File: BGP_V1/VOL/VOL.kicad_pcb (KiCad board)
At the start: 2 copper layers, 60 x 30 mm, 33 parts, among them IC1 TC7660SO-08, P1 CONN_01X03, P2 CONN_01X02, P3 CONN_01X05, P4 CONN_01X05, P5 CONN_01X05, P6 Conn_01x14, P7 CONN_02X02, U1 OPA2170

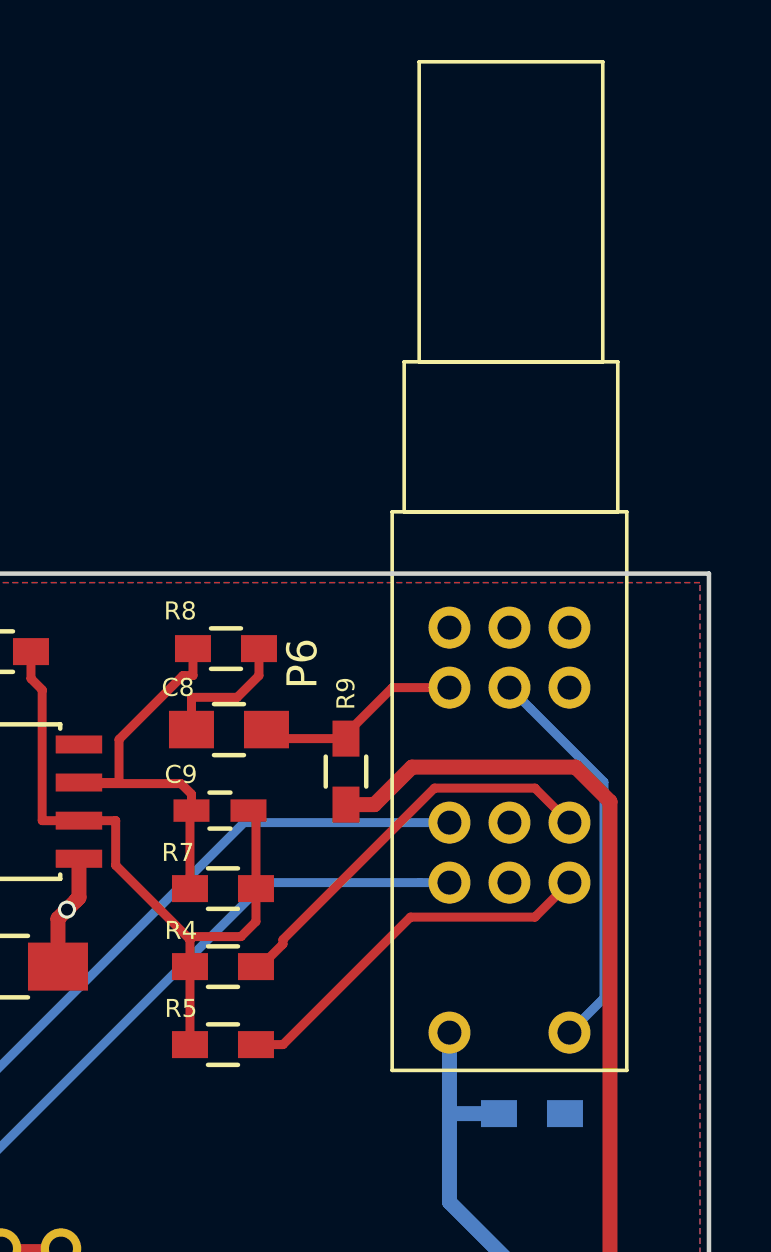
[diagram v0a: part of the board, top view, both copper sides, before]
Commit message: Pot fixups for silkscreen overlap
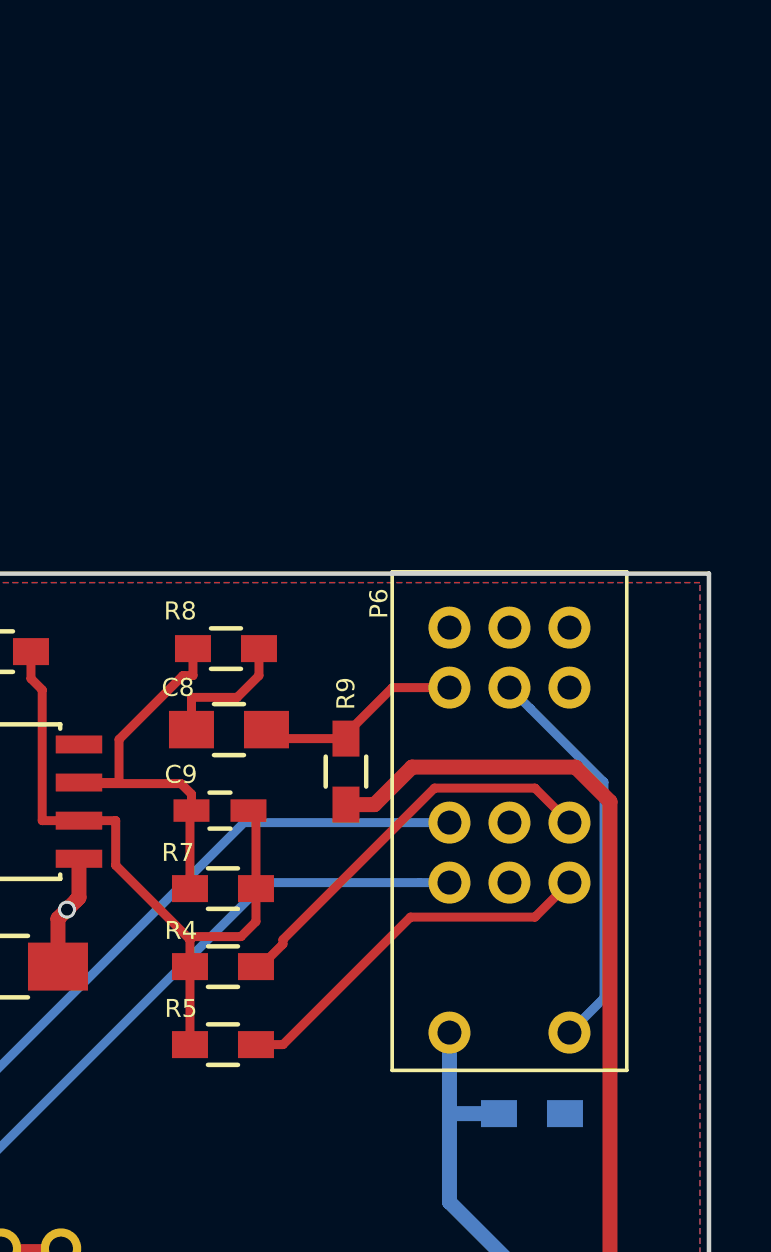
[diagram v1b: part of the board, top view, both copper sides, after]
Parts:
- moved P6 4.25 mm to (174.3, 82.8)
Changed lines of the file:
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@@
     (links 70)
     (no_connects 0)
-    (area 118.924999 63.424999 179.303001 112.85588)
+    (area 118.924999 80.424999 179.303001 112.85588)
     (thickness 1.6)
     (drawings 9)
@@
       (drillshape 0)
       (scaleselection 1)
-      (outputdirectory ../../BGP/GERBER/VOL/))
+      (outputdirectory ../../GERBER/VOL_1/))
   )
   (net 0 "")
@@
   )
   (module LIBS:Potentiometer_TT_P08X_Quad_Vertical_Dual_Shaft (layer F.Cu)
-    (at 176.2 79 90)
+    (at 174.3 82.8 90)
     (descr "Potentiometer, vertically mounted, Omeg PC16PU, Omeg PC16PU, Omeg PC16PU, Vishay/Spectrol 248GJ/249GJ Single, Vishay/Spectrol 248GJ/249GJ Single, Vishay/Spectrol 248GJ/249GJ Single, Vishay/Spectrol 248GH/249GH Single, Vishay/Spectrol 148/149 Single, Vishay/Spectrol 148/149 Single, Vishay/Spectrol 148/149 Single, Vishay/Spectrol 148A/149A Single with mounting plates, Vishay/Spectrol 148/149 Double, Vishay/Spectrol 148A/149A Double with mounting plates, Piher PC-16 Single, Piher PC-16 Single, Piher PC-16 Single, Piher PC-16SV Single, Piher PC-16 Double, Piher PC-16 Triple, Piher T16H Single, Piher T16L Single, Piher T16H Double, Alps RK163 Single, Alps RK163 Double, Alps RK097 Single, Alps RK097 Double, http://www.alps.com/prod/info/E/HTML/Potentiometer/RotaryPotentiometers/RK097/RK09712100AV.html")
     (tags "Potentiometer vertical  Omeg PC16PU  Omeg PC16PU  Omeg PC16PU  Vishay/Spectrol 248GJ/249GJ Single  Vishay/Spectrol 248GJ/249GJ Single  Vishay/Spectrol 248GJ/249GJ Single  Vishay/Spectrol 248GH/249GH Single  Vishay/Spectrol 148/149 Single  Vishay/Spectrol 148/149 Single  Vishay/Spectrol 148/149 Single  Vishay/Spectrol 148A/149A Single with mounting plates  Vishay/Spectrol 148/149 Double  Vishay/Spectrol 148A/149A Double with mounting plates  Piher PC-16 Single  Piher PC-16 Single  Piher PC-16 Single  Piher PC-16SV Single  Piher PC-16 Double  Piher PC-16 Triple  Piher T16H Single  Piher T16L Single  Piher T16H Double  Alps RK163 Single  Alps RK163 Double  Alps RK097 Single  Alps RK097 Double Dual Shaft")
-    (fp_text reference P6 (at -5 -10.75 90) (layer F.SilkS)
-      (effects (font (size 1 1) (thickness 0.15)))
-    )
-    (fp_text value Conn_01x14 (at -5 1.25 90) (layer F.Fab) hide
-      (effects (font (size 1 1) (thickness 0.15)))
-    )
-    (fp_line (start -18.5 -7.7) (end -18.5 0) (layer F.Fab) (width 0.1))
-    (fp_line (start -18.5 0) (end 0 0) (layer F.Fab) (width 0.1))
-    (fp_line (start 0 0) (end 0 -7.7) (layer F.Fab) (width 0.1))
-    (fp_line (start 0 -7.7) (end -18.5 -7.7) (layer F.Fab) (width 0.1))
-    (fp_line (start 0 -7.3) (end 0 -0.3) (layer F.Fab) (width 0.1))
-    (fp_line (start 0 -0.3) (end 5 -0.3) (layer F.Fab) (width 0.1))
-    (fp_line (start 5 -0.3) (end 5 -7.3) (layer F.Fab) (width 0.1))
-    (fp_line (start 5 -7.3) (end 0 -7.3) (layer F.Fab) (width 0.1))
-    (fp_line (start 5 -6.8) (end 5 -0.8) (layer F.Fab) (width 0.1))
-    (fp_line (start 5 -0.8) (end 15 -0.8) (layer F.Fab) (width 0.1))
-    (fp_line (start 15 -0.8) (end 15 -6.8) (layer F.Fab) (width 0.1))
-    (fp_line (start 15 -6.8) (end 5 -6.8) (layer F.Fab) (width 0.1))
-    (fp_line (start -18.56 -7.76) (end 0.06 -7.76) (layer F.SilkS) (width 0.12))
-    (fp_line (start -18.56 0.06) (end 0.06 0.06) (layer F.SilkS) (width 0.12))
-    (fp_line (start -18.56 -7.76) (end -18.56 0.06) (layer F.SilkS) (width 0.12))
-    (fp_line (start 0.06 -7.76) (end 0.06 0.06) (layer F.SilkS) (width 0.12))
-    (fp_line (start 0.06 -7.36) (end 5.06 -7.36) (layer F.SilkS) (width 0.12))
-    (fp_line (start 0.06 -0.24) (end 5.06 -0.24) (layer F.SilkS) (width 0.12))
-    (fp_line (start 0.06 -7.36) (end 0.06 -0.24) (layer F.SilkS) (width 0.12))
-    (fp_line (start 5.06 -7.36) (end 5.06 -0.24) (layer F.SilkS) (width 0.12))
-    (fp_line (start 5.06 -6.86) (end 15.06 -6.86) (layer F.SilkS) (width 0.12))
-    (fp_line (start 5.06 -0.74) (end 15.06 -0.74) (layer F.SilkS) (width 0.12))
-    (fp_line (start 5.06 -6.86) (end 5.06 -0.74) (layer F.SilkS) (width 0.12))
-    (fp_line (start 15.06 -6.86) (end 15.06 -0.74) (layer F.SilkS) (width 0.12))
-    (fp_line (start -18.89 -8.09) (end -18.89 0.25) (layer F.CrtYd) (width 0.05))
-    (fp_line (start -18.89 0.25) (end 15.25 0.25) (layer F.CrtYd) (width 0.05))
-    (fp_line (start 15.25 0.25) (end 15.25 -8.09) (layer F.CrtYd) (width 0.05))
-    (fp_line (start 15.25 -8.09) (end -18.89 -8.09) (layer F.CrtYd) (width 0.05))
-    (pad 3 thru_hole circle (at -3.8 -5.85 90) (size 1.4 1.4) (drill 0.8) (layers *.Cu *.Mask)
+    (fp_text reference P6 (at 0.8 -6.3 90) (layer F.SilkS)
+      (effects (font (size 0.6 0.6) (thickness 0.15)))
+    )
+    (fp_text value Conn_01x14 (at -1.2 3.15 90) (layer F.Fab) hide
+      (effects (font (size 0.6 0.6) (thickness 0.15)))
+    )
+    (fp_line (start -14.7 -5.8) (end -14.7 1.9) (layer F.Fab) (width 0.1))
+    (fp_line (start -14.7 1.9) (end 1.8 1.9) (layer F.Fab) (width 0.1))
+    (fp_line (start 1.8 1.9) (end 1.8 -5.8) (layer F.Fab) (width 0.1))
+    (fp_line (start 1.8 -5.8) (end -14.7 -5.8) (layer F.Fab) (width 0.1))
+    (fp_line (start -14.76 -5.86) (end 1.86 -5.86) (layer F.SilkS) (width 0.12))
+    (fp_line (start -14.76 1.96) (end 1.86 1.96) (layer F.SilkS) (width 0.12))
+    (fp_line (start -14.76 -5.86) (end -14.76 1.96) (layer F.SilkS) (width 0.12))
+    (fp_line (start 1.86 -5.86) (end 1.86 1.96) (layer F.SilkS) (width 0.12))
+    (fp_line (start -15.09 -6.19) (end -15.09 2.15) (layer F.CrtYd) (width 0.05))
+    (fp_line (start -15.09 2.15) (end 2.05 2.15) (layer F.CrtYd) (width 0.05))
+    (fp_line (start 2.05 2.15) (end 2.05 -6.19) (layer F.CrtYd) (width 0.05))
+    (fp_line (start 2.05 -6.19) (end -15.09 -6.19) (layer F.CrtYd) (width 0.05))
+    (pad 3 thru_hole circle (at 0 -3.95 90) (size 1.4 1.4) (drill 0.8) (layers *.Cu *.Mask)
       (net 29 "Net-(P6-Pad3)"))
-    (pad 2 thru_hole circle (at -3.8 -3.85 90) (size 1.4 1.4) (drill 0.8) (layers *.Cu *.Mask)
+    (pad 2 thru_hole circle (at 0 -1.95 90) (size 1.4 1.4) (drill 0.8) (layers *.Cu *.Mask)
       (net 30 "Net-(P6-Pad2)"))
-    (pad 13 thru_hole circle (at -17.3 -1.85 90) (size 1.4 1.4) (drill 0.8) (layers *.Cu *.Mask)
+    (pad 13 thru_hole circle (at -13.5 0.05 90) (size 1.4 1.4) (drill 0.8) (layers *.Cu *.Mask)
       (net 32 /VP_OUT))
-    (pad 1 thru_hole circle (at -3.8 -1.85 90) (size 1.4 1.4) (drill 0.8) (layers *.Cu *.Mask)
+    (pad 1 thru_hole circle (at 0 0.05 90) (size 1.4 1.4) (drill 0.8) (layers *.Cu *.Mask)
       (net 31 "Net-(P6-Pad1)"))
-    (pad 11 thru_hole circle (at -12.3 -3.85 90) (size 1.4 1.4) (drill 0.8) (layers *.Cu *.Mask)
-      (net 4 Earth))
-    (pad 14 thru_hole circle (at -17.3 -5.85 90) (size 1.4 1.4) (drill 0.8) (layers *.Cu *.Mask)
+    (pad 11 thru_hole circle (at -8.5 -1.95 90) (size 1.4 1.4) (drill 0.8) (layers *.Cu *.Mask)
+      (net 4 Earth))
+    (pad 14 thru_hole circle (at -13.5 -3.95 90) (size 1.4 1.4) (drill 0.8) (layers *.Cu *.Mask)
       (net 13 /OUT))
-    (pad 4 thru_hole circle (at -5.8 -1.85 90) (size 1.4 1.4) (drill 0.8) (layers *.Cu *.Mask)
-      (net 4 Earth))
-    (pad 5 thru_hole circle (at -5.8 -3.85 90) (size 1.4 1.4) (drill 0.8) (layers *.Cu *.Mask)
+    (pad 4 thru_hole circle (at -2 0.05 90) (size 1.4 1.4) (drill 0.8) (layers *.Cu *.Mask)
+      (net 4 Earth))
+    (pad 5 thru_hole circle (at -2 -1.95 90) (size 1.4 1.4) (drill 0.8) (layers *.Cu *.Mask)
       (net 32 /VP_OUT))
-    (pad 6 thru_hole circle (at -5.8 -5.85 90) (size 1.4 1.4) (drill 0.8) (layers *.Cu *.Mask)
+    (pad 6 thru_hole circle (at -2 -3.95 90) (size 1.4 1.4) (drill 0.8) (layers *.Cu *.Mask)
       (net 28 /VP_1))
-    (pad 7 thru_hole circle (at -10.3 -1.85 90) (size 1.4 1.4) (drill 0.8) (layers *.Cu *.Mask)
+    (pad 7 thru_hole circle (at -6.5 0.05 90) (size 1.4 1.4) (drill 0.8) (layers *.Cu *.Mask)
       (net 22 /VB1_3))
-    (pad 8 thru_hole circle (at -10.3 -3.85 90) (size 1.4 1.4) (drill 0.8) (layers *.Cu *.Mask)
-      (net 4 Earth))
-    (pad 9 thru_hole circle (at -10.3 -5.85 90) (size 1.4 1.4) (drill 0.8) (layers *.Cu *.Mask)
+    (pad 8 thru_hole circle (at -6.5 -1.95 90) (size 1.4 1.4) (drill 0.8) (layers *.Cu *.Mask)
+      (net 4 Earth))
+    (pad 9 thru_hole circle (at -6.5 -3.95 90) (size 1.4 1.4) (drill 0.8) (layers *.Cu *.Mask)
       (net 15 /OUT_B))
-    (pad 10 thru_hole circle (at -12.3 -1.85 90) (size 1.4 1.4) (drill 0.8) (layers *.Cu *.Mask)
+    (pad 10 thru_hole circle (at -8.5 0.05 90) (size 1.4 1.4) (drill 0.8) (layers *.Cu *.Mask)
       (net 21 /VB2_3))
-    (pad 12 thru_hole circle (at -12.3 -5.85 90) (size 1.4 1.4) (drill 0.8) (layers *.Cu *.Mask)
+    (pad 12 thru_hole circle (at -8.5 -3.95 90) (size 1.4 1.4) (drill 0.8) (layers *.Cu *.Mask)
       (net 17 /OUT_N))
     (model Potentiometers.3dshapes/Potentiometer_Alps_RK097_Double_Vertical.wrl

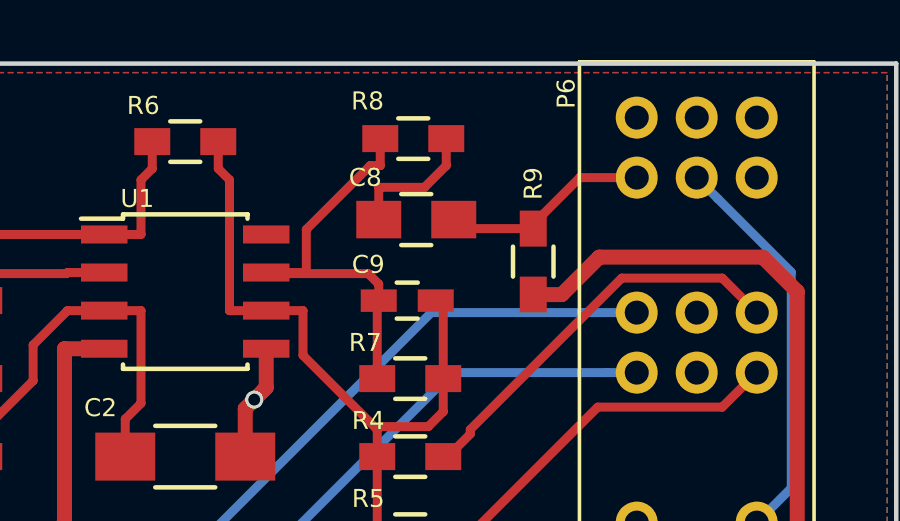
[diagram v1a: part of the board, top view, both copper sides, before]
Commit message: Further component refinement in V1
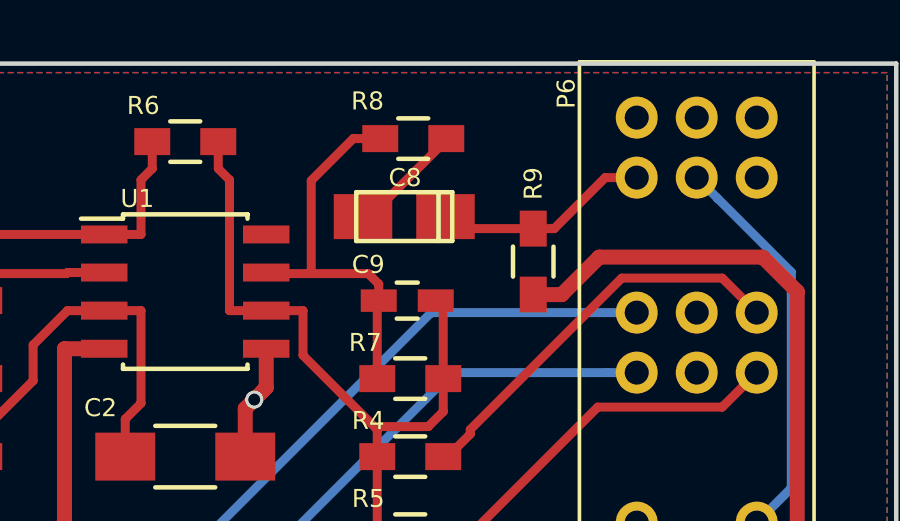
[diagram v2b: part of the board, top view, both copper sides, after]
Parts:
- C8: footprint Capacitors_SMD:C_0805_HandSoldering -> Capacitors_Tantalum_SMD:TantalC_SizeS_EIA-3216
- moved C8 0.41 mm to (162.6, 86.1), turned to 0 degrees
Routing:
- net Net-(C9-Pad1): track 14.2 -> 13.1 mm
- net Net-(C8-Pad2): track 4.53 -> 3.88 mm
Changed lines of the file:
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@@
     (thickness 1.6)
     (drawings 9)
-    (tracks 244)
+    (tracks 241)
     (zones 0)
     (modules 33)
@@
     )
   )
-  (module Capacitors_SMD:C_0805_HandSoldering (layer F.Cu)
-    (at 163 86.2 180)
-    (descr "Capacitor SMD 0805, hand soldering")
-    (tags "capacitor 0805")
-    (attr smd)
-    (fp_text reference C8 (at 1.7 1.4 180) (layer F.SilkS)
-      (effects (font (size 0.6 0.6) (thickness 0.15)))
-    )
-    (fp_text value 22u (at 0 2.1 180) (layer F.Fab) hide
-      (effects (font (size 0.6 0.6) (thickness 0.15)))
-    )
-    (fp_line (start -2.3 -1) (end 2.3 -1) (layer F.CrtYd) (width 0.05))
-    (fp_line (start -2.3 1) (end 2.3 1) (layer F.CrtYd) (width 0.05))
-    (fp_line (start -2.3 -1) (end -2.3 1) (layer F.CrtYd) (width 0.05))
-    (fp_line (start 2.3 -1) (end 2.3 1) (layer F.CrtYd) (width 0.05))
-    (fp_line (start 0.5 -0.85) (end -0.5 -0.85) (layer F.SilkS) (width 0.15))
-    (fp_line (start -0.5 0.85) (end 0.5 0.85) (layer F.SilkS) (width 0.15))
-    (pad 1 smd rect (at -1.25 0 180) (size 1.5 1.25) (layers F.Cu F.Paste F.Mask)
-      (net 28 /VP_1))
-    (pad 2 smd rect (at 1.25 0 180) (size 1.5 1.25) (layers F.Cu F.Paste F.Mask)
-      (net 10 "Net-(C8-Pad2)"))
-    (model Capacitors_SMD.3dshapes/C_0805_HandSoldering.wrl
-      (at (xyz 0 0 0))
-      (scale (xyz 1 1 1))
-      (rotate (xyz 0 0 0))
-    )
-  )
   (module Diodes_SMD:SOD-123 (layer F.Cu)
     (at 140.6 90.5 180)
@@
       (at (xyz 0 0 0))
       (scale (xyz 0.393701 0.393701 0.393701))
+      (rotate (xyz 0 0 0))
+    )
+  )
+  (module Capacitors_Tantalum_SMD:TantalC_SizeS_EIA-3216 (layer F.Cu)
+    (at 162.6 86.1)
+    (descr "Tantal Cap. , Size S, EIA-3216, Hand Soldering")
+    (fp_text reference C8 (at 0.0254 -1.2954) (layer F.SilkS)
+      (effects (font (size 0.6 0.6) (thickness 0.15)))
+    )
+    (fp_text value 22u (at 0 1.27) (layer F.Fab)
+      (effects (font (size 0.6 0.6) (thickness 0.15)))
+    )
+    (fp_line (start 1.143 0.8128) (end 1.143 -0.8128) (layer F.SilkS) (width 0.15))
+    (fp_line (start -1.6002 -0.8128) (end -1.6002 0.8128) (layer F.SilkS) (width 0.15))
+    (fp_line (start -1.6002 0.8128) (end 1.6002 0.8128) (layer F.SilkS) (width 0.15))
+    (fp_line (start 1.6002 0.8128) (end 1.6002 -0.8128) (layer F.SilkS) (width 0.15))
+    (fp_line (start 1.6002 -0.8128) (end -1.6002 -0.8128) (layer F.SilkS) (width 0.15))
+    (pad 1 smd rect (at 1.37414 0) (size 1.95072 1.50114) (layers F.Cu F.Paste F.Mask)
+      (net 28 /VP_1))
+    (pad 2 smd rect (at -1.37414 0) (size 1.95072 1.50114) (layers F.Cu F.Paste F.Mask)
+      (net 10 "Net-(C8-Pad2)"))
+    (model Capacitors_Tantalum_SMD.3dshapes/TantalC_SizeS_EIA-3216.wrl
+      (at (xyz 0 0 0))
+      (scale (xyz 1 1 1))
       (rotate (xyz 0 0 0))
     )
@@
   (segment (start 144 103.6) (end 151.2747 96.3253) (width 0.5) (layer F.Cu) (net 8))
   (segment (start 152.6 90.505) (end 151.2747 90.505) (width 0.5) (layer F.Cu) (net 8))
-  (segment (start 163.2756 85.1247) (end 161.75 85.1247) (width 0.3) (layer F.Cu) (net 10))
-  (segment (start 164 84.4003) (end 163.2756 85.1247) (width 0.3) (layer F.Cu) (net 10))
-  (segment (start 164 83.5) (end 164 84.4003) (width 0.3) (layer F.Cu) (net 10))
-  (segment (start 161.75 86.2) (end 161.75 85.1247) (width 0.3) (layer F.Cu) (net 10))
+  (segment (start 161.22586 86.1) (end 161.45065 86.1) (width 0.3) (layer F.Cu) (net 10))
+  (segment (start 161.45065 86.1) (end 164 83.55065) (width 0.3) (layer F.Cu) (net 10))
+  (segment (start 164 83.55065) (end 164 83.5) (width 0.3) (layer F.Cu) (net 10))
   (segment (start 172 99) (end 170.4 99) (width 0.5) (layer B.Cu) (net 13))
   (segment (start 170.4 99) (end 170.35 98.95) (width 0.5) (layer B.Cu) (net 13))
@@
   (segment (start 146.4 87.9997) (end 147.7047 86.695) (width 0.3) (layer F.Cu) (net 24))
   (segment (start 146.4 88.9) (end 146.4 87.9997) (width 0.3) (layer F.Cu) (net 24))
-  (segment (start 157.9 88) (end 161.4 88) (width 0.3) (layer F.Cu) (net 25))
+  (segment (start 157.9 88) (end 159.5 88) (width 0.3) (layer F.Cu) (net 25))
+  (segment (start 159.5 88) (end 161.4 88) (width 0.3) (layer F.Cu) (net 25))
+  (segment (start 161.8 83.5) (end 160.9 83.5) (width 0.3) (layer F.Cu) (net 25))
+  (segment (start 160.9 83.5) (end 159.5 84.9) (width 0.3) (layer F.Cu) (net 25))
+  (segment (start 159.5 84.9) (end 159.5 88) (width 0.3) (layer F.Cu) (net 25))
   (segment (start 161.4 88) (end 161.75 88.35) (width 0.3) (layer F.Cu) (net 25))
   (segment (start 161.75 88.35) (end 161.75 88.9) (width 0.3) (layer F.Cu) (net 25))
@@
   (segment (start 161.75 88.95) (end 161.7 89) (width 0.3) (layer F.Cu) (net 25))
   (segment (start 161.7 89) (end 161.7 91.5) (width 0.3) (layer F.Cu) (net 25))
-  (segment (start 158 87.965) (end 159.2253 87.965) (width 0.3) (layer F.Cu) (net 25))
-  (segment (start 159.335 87.965) (end 159.2253 87.965) (width 0.3) (layer F.Cu) (net 25))
-  (segment (start 159.335 86.5277) (end 159.335 87.965) (width 0.3) (layer F.Cu) (net 25))
-  (segment (start 161.4624 84.4003) (end 159.335 86.5277) (width 0.3) (layer F.Cu) (net 25))
-  (segment (start 161.8 84.4003) (end 161.4624 84.4003) (width 0.3) (layer F.Cu) (net 25))
-  (segment (start 161.8 83.5) (end 161.8 84.4003) (width 0.3) (layer F.Cu) (net 25))
   (segment (start 163.9 91.5) (end 163.9 92.6) (width 0.3) (layer F.Cu) (net 26))
   (segment (start 163.9 92.6) (end 163.4 93.1) (width 0.3) (layer F.Cu) (net 26))
@@
   (segment (start 139.35 93.0247) (end 140.7747 91.6) (width 0.3) (layer F.Cu) (net 27))
   (segment (start 141.85 87) (end 141.85 88.0753) (width 0.3) (layer F.Cu) (net 27))
-  (segment (start 166.9 86.5) (end 164.55 86.5) (width 0.3) (layer F.Cu) (net 28))
-  (segment (start 164.55 86.5) (end 164.25 86.2) (width 0.3) (layer F.Cu) (net 28))
-  (segment (start 170.35 84.8) (end 168.45 84.8) (width 0.3) (layer F.Cu) (net 28))
-  (segment (start 168.45 84.8) (end 166.9 86.35) (width 0.3) (layer F.Cu) (net 28))
-  (segment (start 166.9 86.35) (end 166.9 86.5) (width 0.3) (layer F.Cu) (net 28))
+  (segment (start 163.97414 86.1) (end 164.37414 86.5) (width 0.3) (layer F.Cu) (net 28))
+  (segment (start 164.37414 86.5) (end 166.9 86.5) (width 0.3) (layer F.Cu) (net 28))
+  (segment (start 170.35 84.8) (end 169.3 84.8) (width 0.3) (layer F.Cu) (net 28))
+  (segment (start 169.3 84.8) (end 167.6 86.5) (width 0.3) (layer F.Cu) (net 28))
+  (segment (start 167.6 86.5) (end 166.9 86.5) (width 0.3) (layer F.Cu) (net 28))
   (segment (start 174.35 96.3) (end 175.500001 95.149999) (width 0.3) (layer B.Cu) (net 32))
   (segment (start 175.500001 95.149999) (end 175.500001 87.950001) (width 0.3) (layer B.Cu) (net 32))
